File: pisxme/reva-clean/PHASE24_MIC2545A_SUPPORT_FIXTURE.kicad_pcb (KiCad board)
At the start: 2 copper layers, 25 x 20 mm, 7 parts, among them U3 MIC2545A-1YM

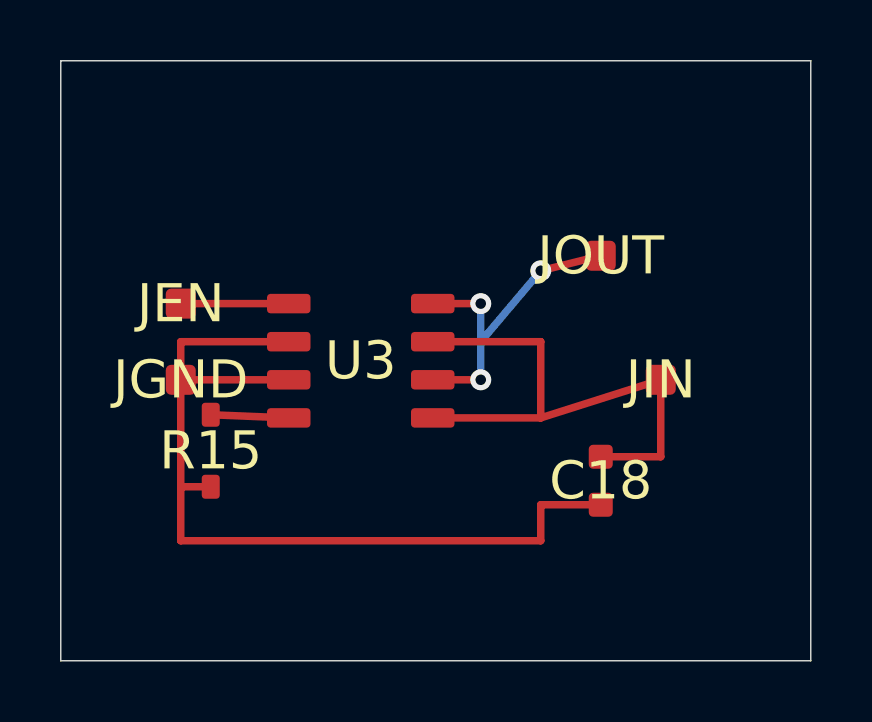
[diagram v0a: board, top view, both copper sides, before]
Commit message: phase24: align MIC2545A fixture with Microchip land pattern
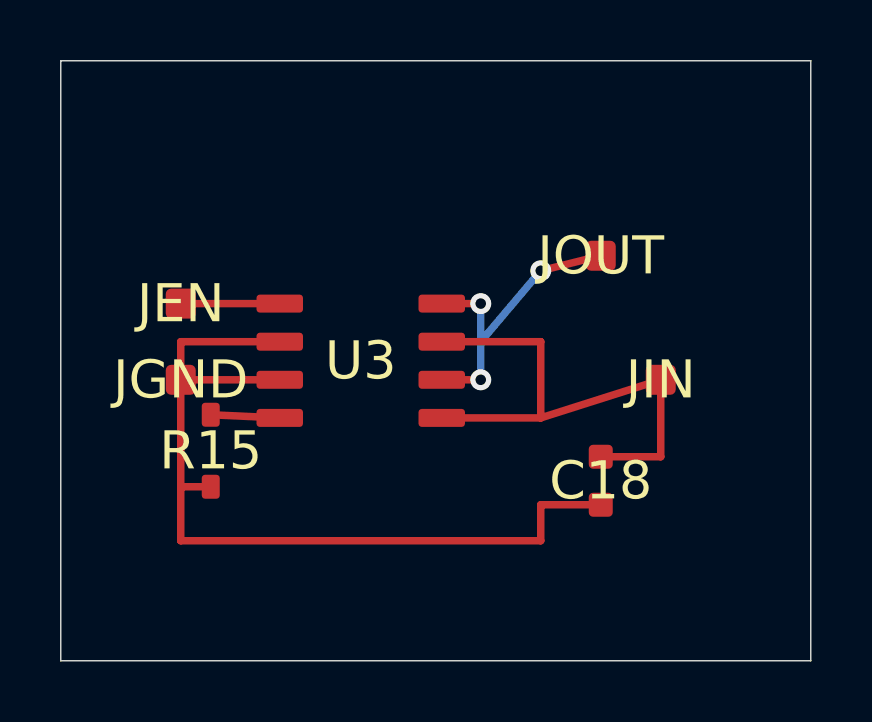
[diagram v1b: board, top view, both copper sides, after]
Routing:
- net SSD_3V3_IN: track 18.5 -> 17.9 mm
- net SSD_3V3: track 10.9 -> 10.3 mm
- net GND: track 30.0 -> 29.4 mm
